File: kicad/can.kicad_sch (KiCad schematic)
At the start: 4 parts, among them U2 TCAN334

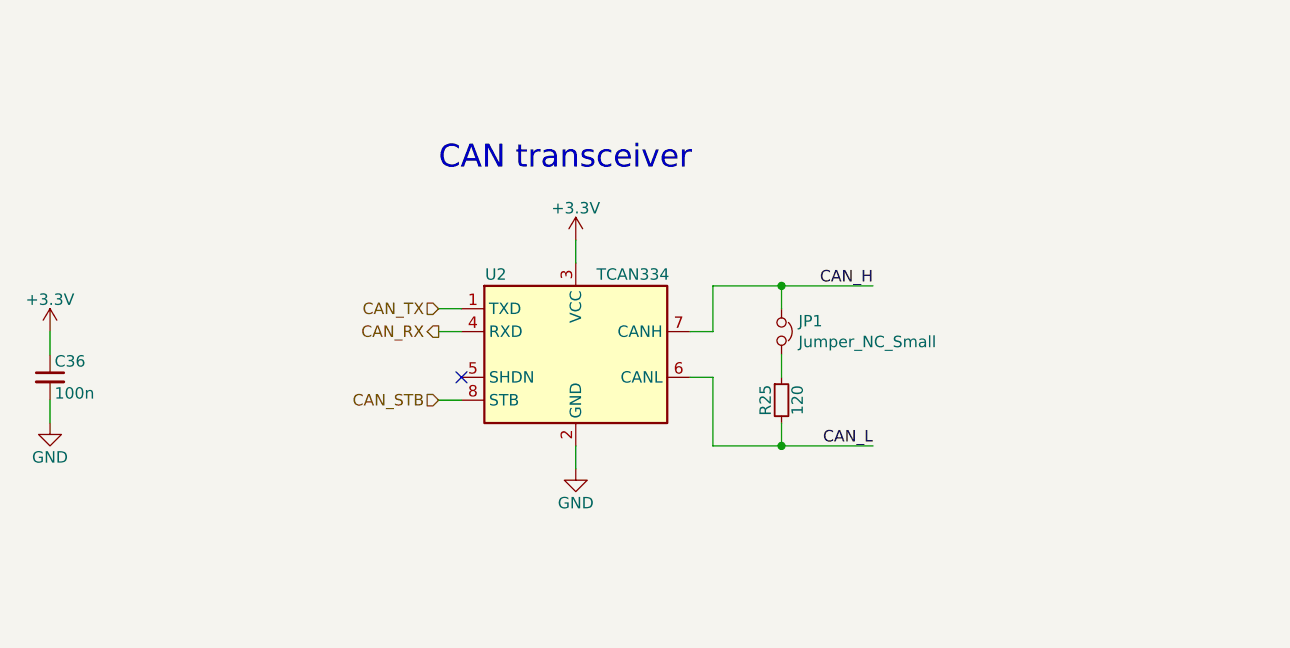
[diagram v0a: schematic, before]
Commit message: WIP: Schematic almost finished
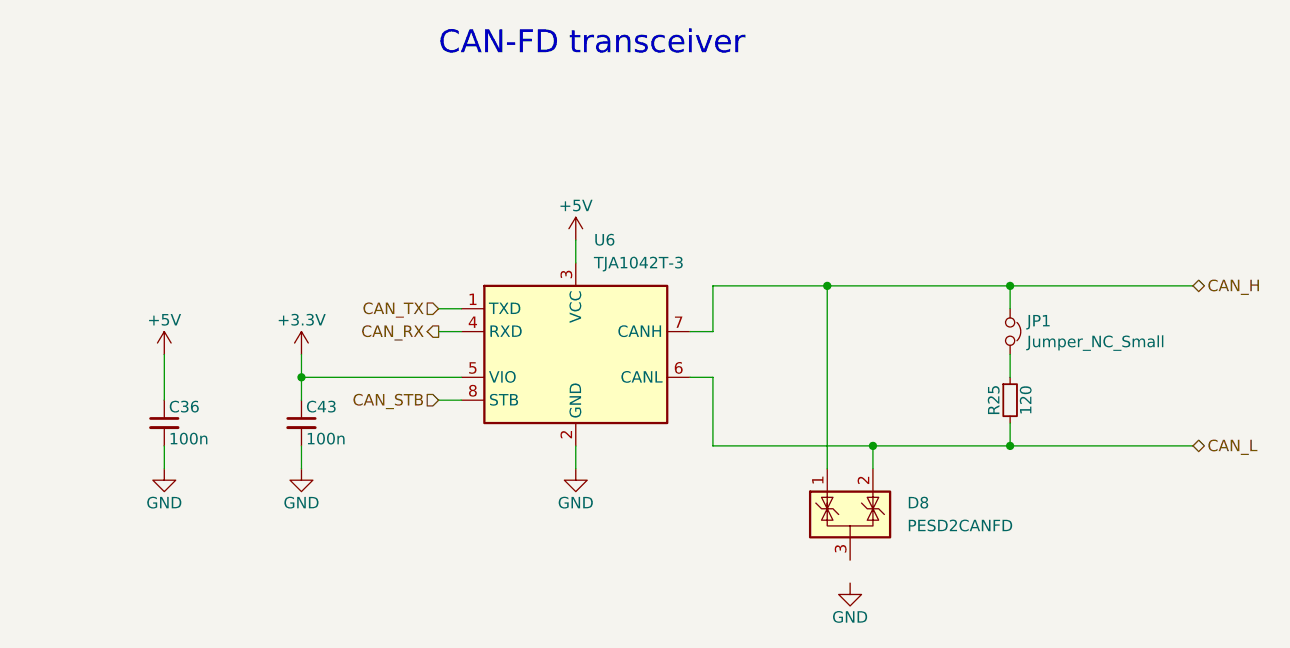
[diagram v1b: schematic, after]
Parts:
- removed U2: TCAN334, LibreSolar:SOIC-8_3.9x4.9mm_Pitch1.27mm, symbol Interface_CAN_LIN:TCAN334
- added C43: 100n, LibreSolar:C_0603_1608, symbol LibreSolar:C
- added D8: PESD2CANFD, Package_TO_SOT_SMD:SOT-23, symbol Power_Protection:NUP2105L
- added U6: TJA1042T-3, Package_SO:SOIC-8_3.9x4.9mm_P1.27mm, symbol Interface_CAN_LIN:TJA1042T-3
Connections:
- net +3V3: now also C43.1, U6.5 (VIO); no longer C36.1
- net CAN_H: now also D8.1 (K), U6.7 (CANH)
- net CAN_L: now also D8.2 (K), U6.6 (CANL)
- net CAN_RX: now also U6.4 (RXD)
- net CAN_STB: now also U6.8 (STB)
- net CAN_TX: now also U6.1 (TXD)
- net GND: now also C43.2, U6.2 (GND)
- new net +5V: C36.1, U6.3 (VCC)
- no-connect marks 1 -> 0
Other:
- note added: "CAN-FD transceiver"
- note removed: "CAN transceiver"
- company: (none) -> Libre Solar Technologies GmbH
- title: (none) -> BMS 16S Control Board
- moved on the sheet: C36, JP1, R25

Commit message: v0.1 design ready for review
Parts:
- removed JP1: Jumper_NC_Small, Connector_PinHeader_2.54mm:PinHeader_1x02_P2.54mm_Vertical, symbol LibreSolar:Jumper_NC_Small
- removed R25: 120, LibreSolar:R_1206_3216, symbol LibreSolar:R
- C36, C43: value 100n -> 100nF; Manufacturer Yageo -> any; PartNumber CC0603KRX7R9BB104 -> (none)
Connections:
- net GND: now also D8.3 (A)
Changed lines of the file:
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@@
   (title_block
     (title "BMS 16S Control Board")
-    (date "2022-01-20")
+    (date "2022-02-24")
     (rev "0.1")
     (company "Libre Solar Technologies GmbH")
     (comment 1 "Website: https://libre.solar")
     (comment 2 "Author: Martin Jäger")
-    (comment 3 "License: Creative Commons Attribution-ShareAlike 4.0 International")
-  )
-  (junction (at 180.34 93.98) (diameter 0.9144) (color 0 0 0 0)
-  )
-  (junction (at 180.34 76.2) (diameter 0) (color 0 0 0 0)
+    (comment 3 "License: CERN-OHL-W")
   )
   (junction (at 160.02 76.2) (diameter 0) (color 0 0 0 0)
@@
   (junction (at 165.1 93.98) (diameter 0) (color 0 0 0 0)
   )
-  (wire (pts (xy 160.02 76.2) (xy 180.34 76.2))
+  (wire (pts (xy 160.02 76.2) (xy 200.66 76.2))
     (stroke (width 0) (type solid) (color 0 0 0 0))
   )
@@
     (stroke (width 0) (type solid) (color 0 0 0 0))
   )
-  (wire (pts (xy 200.66 93.98) (xy 180.34 93.98))
-    (stroke (width 0) (type solid) (color 0 0 0 0))
-  )
   (wire (pts (xy 116.84 81.28) (xy 119.38 81.28))
     (stroke (width 0) (type solid) (color 0 0 0 0))
@@
     (stroke (width 0) (type solid) (color 0 0 0 0))
   )
+  (wire (pts (xy 162.56 106.68) (xy 162.56 109.22))
+    (stroke (width 0) (type default) (color 0 0 0 0))
+  )
   (wire (pts (xy 86.36 96.52) (xy 86.36 93.98))
     (stroke (width 0) (type solid) (color 0 0 0 0))
   )
-  (wire (pts (xy 180.34 93.98) (xy 165.1 93.98))
+  (wire (pts (xy 165.1 93.98) (xy 200.66 93.98))
     (stroke (width 0) (type solid) (color 0 0 0 0))
   )
@@
     (stroke (width 0) (type default) (color 0 0 0 0))
   )
-  (wire (pts (xy 180.34 78.74) (xy 180.34 76.2))
-    (stroke (width 0) (type solid) (color 0 0 0 0))
-  )
   (wire (pts (xy 160.02 76.2) (xy 160.02 96.52))
     (stroke (width 0) (type default) (color 0 0 0 0))
@@
     (stroke (width 0) (type solid) (color 0 0 0 0))
   )
-  (wire (pts (xy 180.34 76.2) (xy 200.66 76.2))
-    (stroke (width 0) (type default) (color 0 0 0 0))
-  )
   (wire (pts (xy 132.08 93.98) (xy 132.08 96.52))
     (stroke (width 0) (type solid) (color 0 0 0 0))
   )
   (wire (pts (xy 165.1 93.98) (xy 147.32 93.98))
-    (stroke (width 0) (type solid) (color 0 0 0 0))
-  )
-  (wire (pts (xy 180.34 93.98) (xy 180.34 91.44))
-    (stroke (width 0) (type solid) (color 0 0 0 0))
-  )
-  (wire (pts (xy 180.34 83.82) (xy 180.34 86.36))
     (stroke (width 0) (type solid) (color 0 0 0 0))
   )
@@
       (effects (font (size 1.27 1.27)) (justify left))
     )
-    (property "Value" "100n" (id 1) (at 86.868 93.218 0)
+    (property "Value" "100nF" (id 1) (at 86.868 93.218 0)
       (effects (font (size 1.27 1.27)) (justify left))
     )
@@
     )
     (property "Datasheet" "" (id 3) (at 86.36 91.44 0))
-    (property "Manufacturer" "Yageo" (id 4) (at -86.36 135.89 0)
+    (property "Manufacturer" "any" (id 4) (at -86.36 135.89 0)
       (effects (font (size 1.27 1.27)) hide)
     )
-    (property "PartNumber" "CC0603KRX7R9BB104" (id 5) (at -86.36 135.89 0)
+    (property "PartNumber" "" (id 5) (at -86.36 135.89 0)
       (effects (font (size 1.27 1.27)) hide)
     )
@@
       (effects (font (size 1.27 1.27)) (justify left))
     )
-    (property "Value" "100n" (id 1) (at 102.108 93.218 0)
+    (property "Value" "100nF" (id 1) (at 102.108 93.218 0)
       (effects (font (size 1.27 1.27)) (justify left))
     )
@@
     )
     (property "Datasheet" "" (id 3) (at 101.6 91.44 0))
-    (property "Manufacturer" "Yageo" (id 4) (at -71.12 135.89 0)
+    (property "Manufacturer" "any" (id 4) (at -71.12 135.89 0)
       (effects (font (size 1.27 1.27)) hide)
     )
-    (property "PartNumber" "CC0603KRX7R9BB104" (id 5) (at -71.12 135.89 0)
-      (effects (font (size 1.27 1.27)) hide)
-    )
-    (pin "1")
-    (pin "2")
-  )
-  (symbol (lib_id "LibreSolar:R") (at 180.34 88.9 0) (unit 1)
-    (in_bom yes) (on_board yes)
-    (property "Reference" "R25" (id 0) (at 178.562 88.9 90))
-    (property "Value" "120" (id 1) (at 182.118 88.9 90))
-    (property "Footprint" "LibreSolar:R_1206_3216" (id 2) (at 180.34 88.9 0)
-      (effects (font (size 1.27 1.27)) hide)
-    )
-    (property "Datasheet" "" (id 3) (at 180.34 88.9 0))
-    (property "Manufacturer" "Yageo" (id 4) (at -60.96 134.62 0)
-      (effects (font (size 1.27 1.27)) hide)
-    )
-    (property "PartNumber" "RC1206FR-07120RL" (id 5) (at -60.96 134.62 0)
+    (property "PartNumber" "" (id 5) (at -71.12 135.89 0)
       (effects (font (size 1.27 1.27)) hide)
     )
@@
     (pin "8")
   )
-  (symbol (lib_id "LibreSolar:Jumper_NC_Small") (at 180.34 81.28 270) (unit 1)
-    (in_bom yes) (on_board yes)
-    (property "Reference" "JP1" (id 0) (at 182.2196 80.1116 90)
-      (effects (font (size 1.27 1.27)) (justify left))
-    )
-    (property "Value" "Jumper_NC_Small" (id 1) (at 182.2196 82.423 90)
-      (effects (font (size 1.27 1.27)) (justify left))
-    )
-    (property "Footprint" "Connector_PinHeader_2.54mm:PinHeader_1x02_P2.54mm_Vertical" (id 2) (at 180.34 81.28 0)
-      (effects (font (size 1.27 1.27)) hide)
-    )
-    (property "Datasheet" "~" (id 3) (at 180.34 81.28 0)
-      (effects (font (size 1.27 1.27)) hide)
-    )
-    (pin "1")
-    (pin "2")
-  )
   (symbol (lib_id "Power_Protection:NUP2105L") (at 162.56 101.6 0) (unit 1)
